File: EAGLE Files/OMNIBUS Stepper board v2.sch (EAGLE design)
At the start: 52 parts, among them IC1 REG1117, K7 691131710005, K8 691131710005, K9 691131710005, Q1 BTS134D, U2 L7805ACD2T-TR

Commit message: PCB Bugfixes and polishing
• DRV Shield had an routing error (laser indicator LED) also R3 had a wrong value
• New Footprint for the 0.33uF Caps
• Silkscreen polishing
• almost all LEDs are 0805 package now
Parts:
- R3: value 10k -> 470
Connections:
- net L_SW: now also D2.C, Q1.D; no longer D2.A, J1.3
- net N$4: now also D2.A, J1.3; no longer D2.C, Q1.D
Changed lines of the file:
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@@
 <part name="K8" library="Wurth_Terminal_Blocks_Connectors_rev15d" deviceset="691131710005" device=""/>
 <part name="K9" library="Wurth_Terminal_Blocks_Connectors_rev15d" deviceset="691131710005" device=""/>
-<part name="R3" library="rcl" library_urn="urn:adsk.eagle:library:334" deviceset="R-EU_" device="R0805" package3d_urn="urn:adsk.eagle:package:23553/2" value="10k"/>
+<part name="R3" library="rcl" library_urn="urn:adsk.eagle:library:334" deviceset="R-EU_" device="R0805" package3d_urn="urn:adsk.eagle:package:23553/2" value="470"/>
 <part name="R1" library="rcl" library_urn="urn:adsk.eagle:library:334" deviceset="R-EU_" device="R0805" package3d_urn="urn:adsk.eagle:package:23553/2" value="1k"/>
 <part name="R2" library="rcl" library_urn="urn:adsk.eagle:library:334" deviceset="R-EU_" device="R0805" package3d_urn="urn:adsk.eagle:package:23553/2" value="10k"/>
@@
 <net name="L_SW" class="1">
 <segment>
-<label x="218.44" y="144.78" size="1.778" layer="95" rot="R270" xref="yes"/>
-<wire x1="218.44" y1="144.78" x2="210.82" y2="144.78" width="0.1524" layer="91"/>
-<wire x1="210.82" y1="144.78" x2="210.82" y2="132.08" width="0.1524" layer="91"/>
-<pinref part="D2" gate="G$1" pin="A"/>
 <pinref part="LASER-ON" gate="G$1" pin="C"/>
-<wire x1="187.96" y1="132.08" x2="210.82" y2="132.08" width="0.1524" layer="91"/>
-<junction x="210.82" y="132.08"/>
-<pinref part="J1" gate="J$1" pin="3"/>
+<wire x1="187.96" y1="132.08" x2="187.96" y2="124.46" width="0.1524" layer="91"/>
+<wire x1="210.82" y1="121.92" x2="210.82" y2="124.46" width="0.1524" layer="91"/>
+<pinref part="D2" gate="G$1" pin="C"/>
+<pinref part="Q1" gate="G$1" pin="D"/>
+<wire x1="210.82" y1="124.46" x2="210.82" y2="127" width="0.1524" layer="91"/>
+<wire x1="187.96" y1="124.46" x2="210.82" y2="124.46" width="0.1524" layer="91"/>
+<junction x="210.82" y="124.46"/>
 </segment>
 </net>
@@
 <wire x1="226.06" y1="114.3" x2="226.06" y2="106.68" width="0.1524" layer="91"/>
 <label x="226.06" y="106.68" size="1.778" layer="95" rot="R270" xref="yes"/>
-</segment>
-</net>
-<net name="N$4" class="1">
-<segment>
-<wire x1="210.82" y1="121.92" x2="210.82" y2="127" width="0.1524" layer="91"/>
-<pinref part="D2" gate="G$1" pin="C"/>
-<pinref part="Q1" gate="G$1" pin="D"/>
 </segment>
 </net>
@@
 </segment>
 </net>
+<net name="N$4" class="1">
+<segment>
+<pinref part="J1" gate="J$1" pin="3"/>
+<wire x1="218.44" y1="144.78" x2="210.82" y2="144.78" width="0.1524" layer="91"/>
+<wire x1="210.82" y1="144.78" x2="210.82" y2="132.08" width="0.1524" layer="91"/>
+<pinref part="D2" gate="G$1" pin="A"/>
+<label x="218.44" y="144.78" size="1.778" layer="95" rot="R270" xref="yes"/>
+</segment>
+</net>

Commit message: Changed voltage regulators
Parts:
- removed IC1: REG1117, burr-brown:REG1117
- added MIC2954: MIC2954, MIC2954:MIC2954
- C9: device rcl:C-EUC0805 -> rcl:C-EUC1206
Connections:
- net N$4 renamed GND_SW
- net 12V_BD: now also MIC2954.IN; no longer IC1.VIN
- net 5V: now also MIC2954.OUT; no longer IC1.VOUT
- net GND: now also MIC2954.GND@0, MIC2954.GND@1; no longer IC1.GND
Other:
- moved on the sheet: D2, LASER-ON
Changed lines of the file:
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@@
 <part name="C7" library="rcl" library_urn="urn:adsk.eagle:library:334" deviceset="C-EU" device="C0805" package3d_urn="urn:adsk.eagle:package:23617/2" value="100nf"/>
 <part name="D4" library="SS54" deviceset="SS54" device="" value="SS310"/>
-<part name="IC1" library="burr-brown" library_urn="urn:adsk.eagle:library:111" deviceset="REG1117" device="" package3d_urn="urn:adsk.eagle:package:4940/1"/>
 <part name="C4" library="rcl" library_urn="urn:adsk.eagle:library:334" deviceset="C-EU" device="C1206" package3d_urn="urn:adsk.eagle:package:23618/2" value="0.33uf"/>
-<part name="C9" library="rcl" library_urn="urn:adsk.eagle:library:334" deviceset="C-EU" device="C0805" package3d_urn="urn:adsk.eagle:package:23617/2" value="100nf"/>
+<part name="C9" library="rcl" library_urn="urn:adsk.eagle:library:334" deviceset="C-EU" device="C1206" package3d_urn="urn:adsk.eagle:package:23618/2" value="100nf"/>
 <part name="J1" library="SparkFun-Connectors" library_urn="urn:adsk.eagle:library:513" deviceset="CONN_03" device="" package3d_urn="urn:adsk.eagle:package:38063/1"/>
 <part name="Q1" library="FQD7N10LTM" deviceset="FQD7N10LTM" device="" value="BTS134D"/>
@@
 <part name="SUPPLY24" library="Fidget Spinner Example" library_urn="urn:adsk.eagle:library:9489508" deviceset="GND" device=""/>
 <part name="SUPPLY25" library="Fidget Spinner Example" library_urn="urn:adsk.eagle:library:9489508" deviceset="GND" device=""/>
+<part name="MIC2954" library="MIC2954" deviceset="MIC2954" device=""/>
 </parts>
 <sheets>
@@
 <attribute name="VALUE" x="194.818" y="107.95" size="1.778" layer="96" rot="R270"/>
 </instance>
-<instance part="LASER-ON" gate="G$1" x="187.96" y="137.16" smashed="yes">
-<attribute name="NAME" x="191.516" y="132.588" size="1.778" layer="95" rot="R90"/>
-<attribute name="VALUE" x="193.675" y="132.588" size="1.778" layer="96" rot="R90"/>
-</instance>
-<instance part="D2" gate="G$1" x="210.82" y="129.54" smashed="yes" rot="R270">
-<attribute name="NAME" x="211.3026" y="127" size="1.778" layer="95" rot="R270"/>
-<attribute name="VALUE" x="208.5086" y="127" size="1.778" layer="96" rot="R270"/>
+<instance part="LASER-ON" gate="G$1" x="187.96" y="134.62" smashed="yes">
+<attribute name="NAME" x="191.516" y="130.048" size="1.778" layer="95" rot="R90"/>
+<attribute name="VALUE" x="193.675" y="130.048" size="1.778" layer="96" rot="R90"/>
+</instance>
+<instance part="D2" gate="G$1" x="210.82" y="134.62" smashed="yes" rot="R270">
+<attribute name="NAME" x="211.3026" y="132.08" size="1.778" layer="95" rot="R270"/>
+<attribute name="VALUE" x="208.5086" y="132.08" size="1.778" layer="96" rot="R270"/>
 </instance>
 <instance part="C5" gate="G$1" x="106.68" y="256.54" smashed="yes">
@@
 <attribute name="VALUE" x="134.62" y="216.1286" size="1.778" layer="96"/>
 </instance>
-<instance part="IC1" gate="G$1" x="101.6" y="167.64" smashed="yes">
-<attribute name="NAME" x="93.98" y="173.355" size="1.778" layer="95" ratio="10"/>
-<attribute name="VALUE" x="96.52" y="170.18" size="1.778" layer="96" ratio="10"/>
-</instance>
 <instance part="C4" gate="G$1" x="81.28" y="160.02" smashed="yes">
 <attribute name="NAME" x="82.804" y="160.401" size="1.778" layer="95"/>
@@
 <instance part="SUPPLY25" gate="GND" x="198.12" y="91.44" smashed="yes">
 <attribute name="VALUE" x="196.215" y="88.265" size="1.778" layer="96"/>
+</instance>
+<instance part="MIC2954" gate="G$1" x="101.6" y="175.26" smashed="yes">
+<attribute name="NAME" x="91.4236" y="185.4364" size="1.27205" layer="95"/>
+<attribute name="VALUE" x="91.4207" y="182.894490625" size="1.27241875" layer="96"/>
 </instance>
 </instances>
@@
 <wire x1="121.92" y1="154.94" x2="121.92" y2="149.86" width="0.1524" layer="91"/>
 <wire x1="121.92" y1="149.86" x2="101.6" y2="149.86" width="0.1524" layer="91"/>
-<pinref part="IC1" gate="G$1" pin="GND"/>
-<wire x1="101.6" y1="149.86" x2="101.6" y2="154.94" width="0.1524" layer="91"/>
 <pinref part="C4" gate="G$1" pin="2"/>
 <wire x1="81.28" y1="154.94" x2="81.28" y2="149.86" width="0.1524" layer="91"/>
@@
 <wire x1="101.6" y1="149.86" x2="101.6" y2="144.78" width="0.1524" layer="91"/>
 <pinref part="SUPPLY23" gate="GND" pin="GND"/>
+<pinref part="MIC2954" gate="G$1" pin="GND@0"/>
+<wire x1="101.6" y1="162.56" x2="101.6" y2="149.86" width="0.1524" layer="91"/>
+<pinref part="MIC2954" gate="G$1" pin="GND@1"/>
+<junction x="101.6" y="162.56"/>
 </segment>
 <segment>
@@
 <pinref part="C9" gate="G$1" pin="1"/>
 <wire x1="121.92" y1="162.56" x2="121.92" y2="167.64" width="0.1524" layer="91"/>
-<pinref part="IC1" gate="G$1" pin="VOUT"/>
-<wire x1="121.92" y1="167.64" x2="114.3" y2="167.64" width="0.1524" layer="91"/>
+<wire x1="121.92" y1="167.64" x2="116.84" y2="167.64" width="0.1524" layer="91"/>
 <wire x1="121.92" y1="167.64" x2="142.24" y2="167.64" width="0.1524" layer="91"/>
 <junction x="121.92" y="167.64"/>
 <label x="142.24" y="167.64" size="1.778" layer="95" rot="R90" xref="yes"/>
+<pinref part="MIC2954" gate="G$1" pin="OUT"/>
+<wire x1="116.84" y1="175.26" x2="116.84" y2="167.64" width="0.1524" layer="91"/>
 </segment>
 <segment>
@@
 <pinref part="R1" gate="G$1" pin="2"/>
 <pinref part="LASER-ON" gate="G$1" pin="A"/>
-<wire x1="187.96" y1="139.7" x2="187.96" y2="142.24" width="0.1524" layer="91"/>
+<wire x1="187.96" y1="137.16" x2="187.96" y2="142.24" width="0.1524" layer="91"/>
 </segment>
 </net>
@@
 <segment>
 <pinref part="LASER-ON" gate="G$1" pin="C"/>
-<wire x1="187.96" y1="132.08" x2="187.96" y2="124.46" width="0.1524" layer="91"/>
+<wire x1="187.96" y1="129.54" x2="187.96" y2="124.46" width="0.1524" layer="91"/>
 <wire x1="210.82" y1="121.92" x2="210.82" y2="124.46" width="0.1524" layer="91"/>
 <pinref part="D2" gate="G$1" pin="C"/>
 <pinref part="Q1" gate="G$1" pin="D"/>
-<wire x1="210.82" y1="124.46" x2="210.82" y2="127" width="0.1524" layer="91"/>
+<wire x1="210.82" y1="124.46" x2="210.82" y2="132.08" width="0.1524" layer="91"/>
 <wire x1="187.96" y1="124.46" x2="210.82" y2="124.46" width="0.1524" layer="91"/>
 <junction x="210.82" y="124.46"/>
@@
 </segment>
 <segment>
-<pinref part="IC1" gate="G$1" pin="VIN"/>
-<wire x1="88.9" y1="167.64" x2="81.28" y2="167.64" width="0.1524" layer="91"/>
 <pinref part="C4" gate="G$1" pin="1"/>
+<wire x1="86.36" y1="167.64" x2="81.28" y2="167.64" width="0.1524" layer="91"/>
 <wire x1="81.28" y1="167.64" x2="76.2" y2="167.64" width="0.1524" layer="91"/>
 <wire x1="81.28" y1="162.56" x2="81.28" y2="167.64" width="0.1524" layer="91"/>
 <junction x="81.28" y="167.64"/>
 <label x="76.2" y="167.64" size="1.778" layer="95" rot="R180" xref="yes"/>
+<pinref part="MIC2954" gate="G$1" pin="IN"/>
+<wire x1="86.36" y1="175.26" x2="86.36" y2="167.64" width="0.1524" layer="91"/>
 </segment>
 </net>
@@
 </segment>
 </net>
-<net name="N$4" class="1">
+<net name="GND_SW" class="1">
 <segment>
 <pinref part="J1" gate="J$1" pin="3"/>
 <wire x1="218.44" y1="144.78" x2="210.82" y2="144.78" width="0.1524" layer="91"/>
-<wire x1="210.82" y1="144.78" x2="210.82" y2="132.08" width="0.1524" layer="91"/>
+<wire x1="210.82" y1="144.78" x2="210.82" y2="137.16" width="0.1524" layer="91"/>
 <pinref part="D2" gate="G$1" pin="A"/>
 <label x="218.44" y="144.78" size="1.778" layer="95" rot="R270" xref="yes"/>

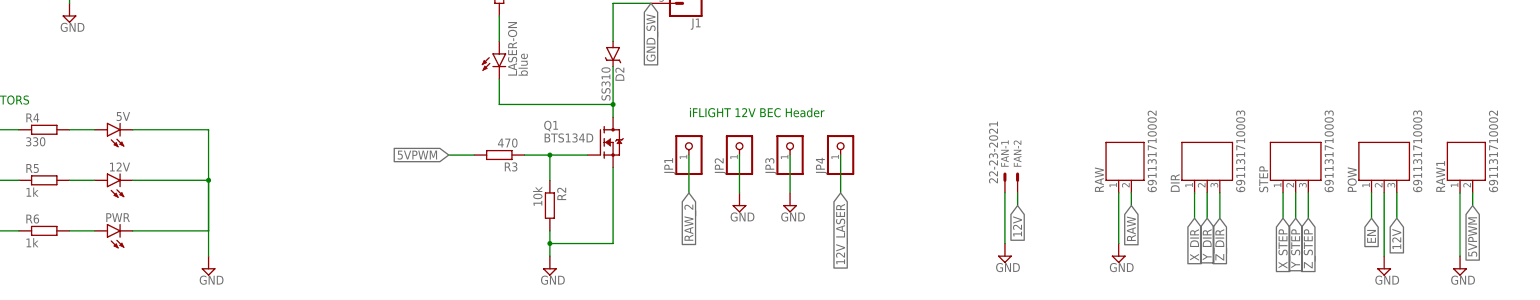
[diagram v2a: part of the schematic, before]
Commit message: clean up
also added BOM
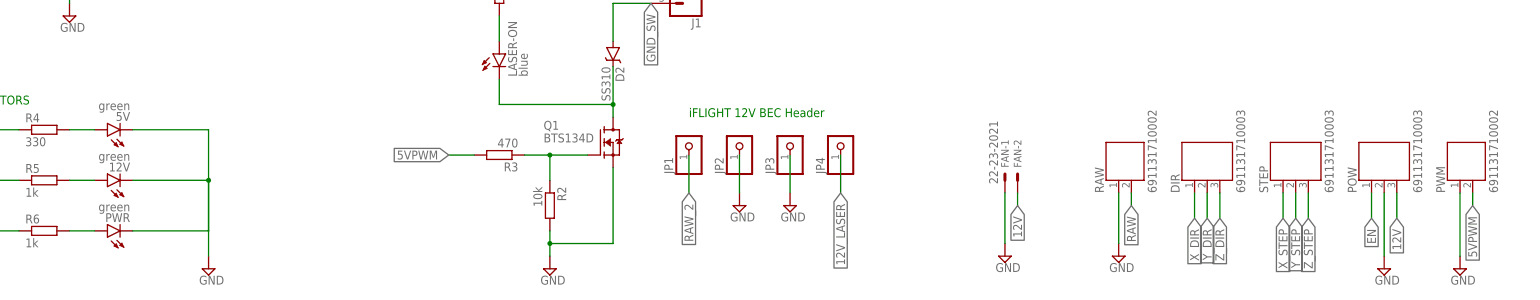
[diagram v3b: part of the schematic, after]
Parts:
- 12V, 5V, PWR: value (none) -> green
- renumbered RAW1 to PWM
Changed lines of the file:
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@@
 <part name="D2" library="SS54" deviceset="SS54" device="" value="SS310"/>
 <part name="C5" library="rcl" library_urn="urn:adsk.eagle:library:334" deviceset="CPOL-EU" device="E5-8.5" package3d_urn="urn:adsk.eagle:package:23374/1" value="100uf 50v"/>
-<part name="RAW1" library="Wurth_Terminal_Blocks_Connectors_rev15d" deviceset="691131710002" device=""/>
+<part name="PWM" library="Wurth_Terminal_Blocks_Connectors_rev15d" deviceset="691131710002" device=""/>
 <part name="R4" library="rcl" library_urn="urn:adsk.eagle:library:334" deviceset="R-EU_" device="R0805" package3d_urn="urn:adsk.eagle:package:23553/2" value="330"/>
-<part name="5V" library="led" library_urn="urn:adsk.eagle:library:259" deviceset="LED" device="CHIPLED_0805" package3d_urn="urn:adsk.eagle:package:15821/2"/>
+<part name="5V" library="led" library_urn="urn:adsk.eagle:library:259" deviceset="LED" device="CHIPLED_0805" package3d_urn="urn:adsk.eagle:package:15821/2" value="green"/>
 <part name="R5" library="rcl" library_urn="urn:adsk.eagle:library:334" deviceset="R-EU_" device="R0805" package3d_urn="urn:adsk.eagle:package:23553/2" value="1k"/>
-<part name="12V" library="led" library_urn="urn:adsk.eagle:library:259" deviceset="LED" device="CHIPLED_0805" package3d_urn="urn:adsk.eagle:package:15821/2"/>
+<part name="12V" library="led" library_urn="urn:adsk.eagle:library:259" deviceset="LED" device="CHIPLED_0805" package3d_urn="urn:adsk.eagle:package:15821/2" value="green"/>
 <part name="R6" library="rcl" library_urn="urn:adsk.eagle:library:334" deviceset="R-EU_" device="R1206" package3d_urn="urn:adsk.eagle:package:23540/2" value="1k"/>
-<part name="PWR" library="led" library_urn="urn:adsk.eagle:library:259" deviceset="LED" device="CHIPLED_0805" package3d_urn="urn:adsk.eagle:package:15821/2"/>
+<part name="PWR" library="led" library_urn="urn:adsk.eagle:library:259" deviceset="LED" device="CHIPLED_0805" package3d_urn="urn:adsk.eagle:package:15821/2" value="green"/>
 <part name="U2" library="L7805ACD2T-TR" deviceset="L7805ACD2T-TR" device=""/>
 <part name="SUPPLY1" library="Fidget Spinner Example" library_urn="urn:adsk.eagle:library:9489508" deviceset="GND" device=""/>
@@
 <attribute name="VALUE" x="107.823" y="251.9426" size="1.778" layer="96"/>
 </instance>
-<instance part="RAW1" gate="G$1" x="381" y="106.68" smashed="yes" rot="R90">
+<instance part="PWM" gate="G$1" x="381" y="106.68" smashed="yes" rot="R90">
 <attribute name="NAME" x="378" y="106.68" size="1.778" layer="95" rot="R90"/>
 <attribute name="VALUE" x="388.62" y="106.68" size="1.778" layer="96" rot="R90"/>
@@
 <segment>
 <wire x1="381" y1="106.68" x2="381" y2="93.98" width="0.1524" layer="91"/>
-<pinref part="RAW1" gate="G$1" pin="1"/>
+<pinref part="PWM" gate="G$1" pin="1"/>
 <pinref part="SUPPLY14" gate="GND" pin="GND"/>
 </segment>
@@
 <wire x1="383.54" y1="106.68" x2="383.54" y2="104.14" width="0.1524" layer="91"/>
 <label x="383.54" y="104.14" size="1.778" layer="95" rot="R270" xref="yes"/>
-<pinref part="RAW1" gate="G$1" pin="2"/>
-</segment>
-<segment>
+<pinref part="PWM" gate="G$1" pin="2"/>
+</segment>
+<segment>
